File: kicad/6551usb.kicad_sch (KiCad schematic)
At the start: 41 parts, among them J1 Conn_01x03_Male, P1 DLP-USB245R, SW1 SW_DIP_x06, U1 74LS04, U10 74LS74, U11 74LS86, U12 74LS33, U13 74LS273, U14 74LS374, U15 74LS244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

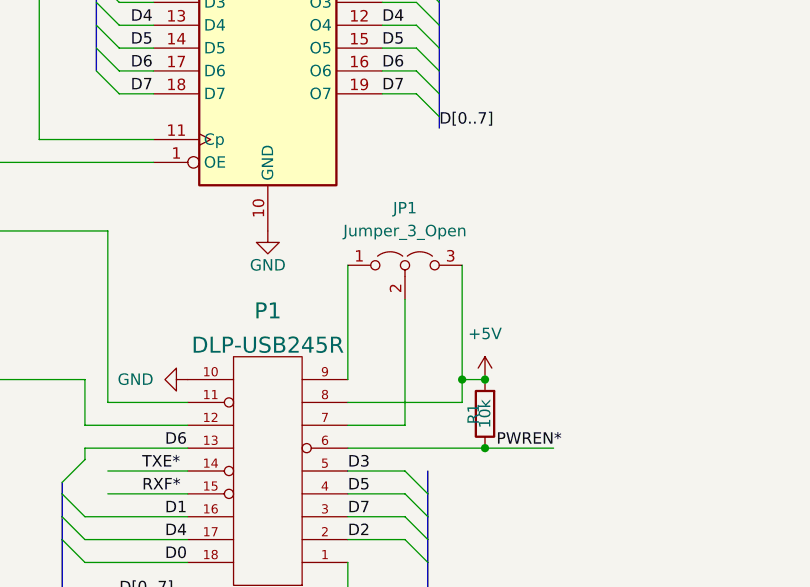
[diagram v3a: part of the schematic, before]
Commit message: Fixed J2 label
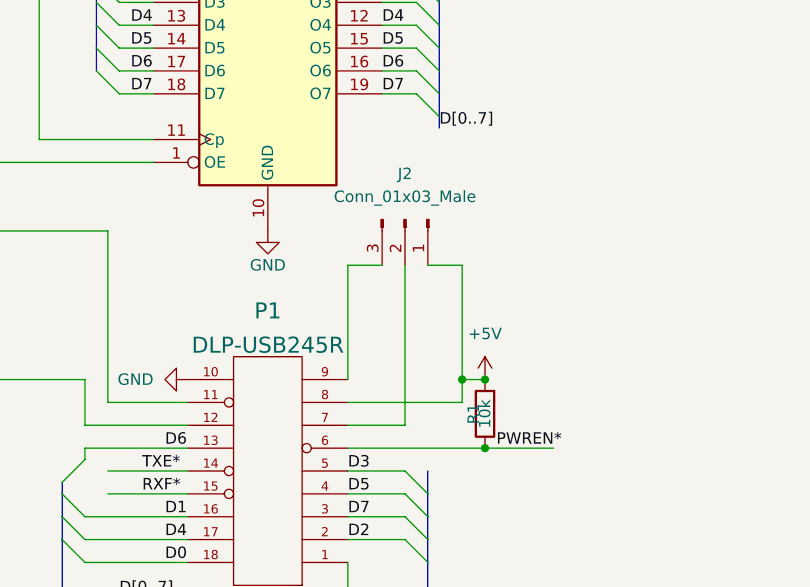
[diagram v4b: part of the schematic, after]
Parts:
- removed JP1: Jumper_3_Open, Connector_PinHeader_2.54mm:PinHeader_1x03_P2.54mm_Vertical, symbol Jumper:Jumper_3_Open
- added J2: Conn_01x03_Male, Connector_PinHeader_2.54mm:PinHeader_1x03_P2.54mm_Vertical, symbol Connector:Conn_01x03_Male
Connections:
- net +5V: now also J2.1 (Pin_1)
- net at P1.9 (PORTVCC): now also J2.3 (Pin_3)
- net at P1.7 (VCCIO): now also J2.2 (Pin_2)
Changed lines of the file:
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@@
     (stroke (width 0) (type default) (color 0 0 0 0))
   )
+  (wire (pts (xy 285.75 67.31) (xy 289.56 67.31))
+    (stroke (width 0) (type default) (color 0 0 0 0))
+  )
   (wire (pts (xy 256.54 95.25) (xy 267.97 95.25))
     (stroke (width 0) (type default) (color 0 0 0 0))
@@
     (stroke (width 0) (type default) (color 0 0 0 0))
   )
+  (wire (pts (xy 294.64 67.31) (xy 298.45 67.31))
+    (stroke (width 0) (type default) (color 0 0 0 0))
+  )
   (bus (pts (xy 254 92.71) (xy 254 95.25))
     (stroke (width 0) (type default) (color 0 0 0 0))
@@
     (stroke (width 0) (type default) (color 0 0 0 0))
   )
-  (wire (pts (xy 292.1 71.12) (xy 292.1 85.09))
+  (wire (pts (xy 292.1 67.31) (xy 292.1 85.09))
     (stroke (width 0) (type default) (color 0 0 0 0))
   )
@@
     (pin "7")
   )
-  (symbol (lib_id "Jumper:Jumper_3_Open") (at 292.1 67.31 0) (unit 1)
-    (in_bom yes) (on_board yes) (fields_autoplaced)
-    (property "Reference" "JP1" (id 0) (at 292.1 60.96 0))
-    (property "Value" "Jumper_3_Open" (id 1) (at 292.1 63.5 0))
-    (property "Footprint" "Connector_PinHeader_2.54mm:PinHeader_1x03_P2.54mm_Vertical" (id 2) (at 292.1 67.31 0)
-      (effects (font (size 1.27 1.27)) hide)
-    )
-    (property "Datasheet" "~" (id 3) (at 292.1 67.31 0)
-      (effects (font (size 1.27 1.27)) hide)
-    )
-    (pin "1")
-    (pin "2")
-    (pin "3")
-  )
   (symbol (lib_id "74xx:74LS00") (at 215.9 45.72 0) (unit 1)
     (in_bom yes) (on_board yes) (fields_autoplaced)
@@
     (pin "1")
   )
+  (symbol (lib_id "Connector:Conn_01x03_Male") (at 292.1 62.23 270) (unit 1)
+    (in_bom yes) (on_board yes) (fields_autoplaced)
+    (property "Reference" "J2" (id 0) (at 292.1 57.15 90))
+    (property "Value" "Conn_01x03_Male" (id 1) (at 292.1 59.69 90))
+    (property "Footprint" "Connector_PinHeader_2.54mm:PinHeader_1x03_P2.54mm_Vertical" (id 2) (at 292.1 62.23 0)
+      (effects (font (size 1.27 1.27)) hide)
+    )
+    (property "Datasheet" "~" (id 3) (at 292.1 62.23 0)
+      (effects (font (size 1.27 1.27)) hide)
+    )
+    (pin "1")
+    (pin "2")
+    (pin "3")
+  )
   (symbol (lib_id "74xx:74LS04") (at 30.48 238.76 0) (unit 5)
     (in_bom yes) (on_board yes) (fields_autoplaced)
@@
       (reference "J1") (unit 1) (value "Conn_01x03_Male") (footprint "Connector_PinHeader_2.54mm:PinHeader_1x03_P2.54mm_Vertical")
     )
-    (path "/8029017d-056a-400b-81cc-fd0942e56f27"
-      (reference "JP1") (unit 1) (value "Jumper_3_Open") (footprint "Connector_PinHeader_2.54mm:PinHeader_1x03_P2.54mm_Vertical")
+    (path "/f2a90eb1-13cf-40f3-9b87-e454685fd87f"
+      (reference "J2") (unit 1) (value "Conn_01x03_Male") (footprint "Connector_PinHeader_2.54mm:PinHeader_1x03_P2.54mm_Vertical")
     )
     (path "/e683bc92-d8a0-46fd-94c4-362ea9e7214a"
